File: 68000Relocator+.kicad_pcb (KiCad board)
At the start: 2 copper layers, 97.4 x 94.7 mm, 5 parts, among them J1 5V AUX, P99 OSHW_LOGO, U1 68000D, U2 68000D

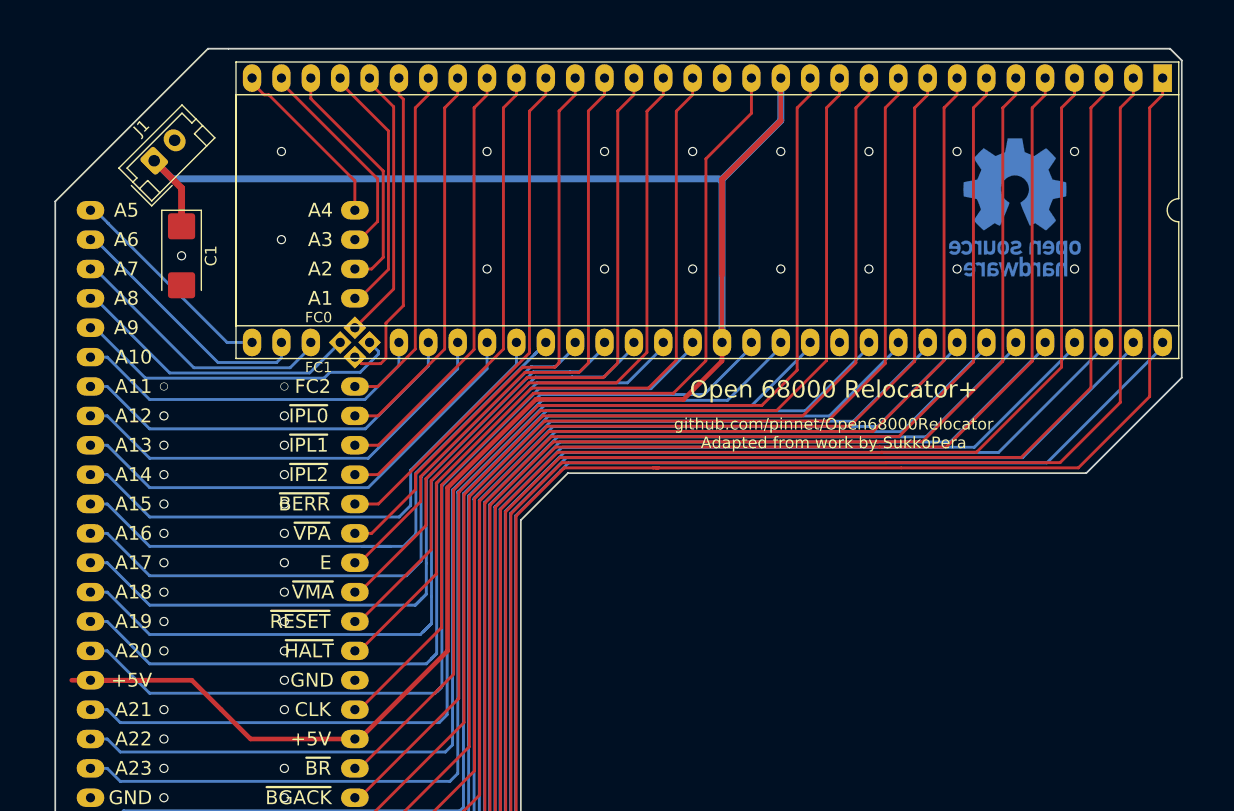
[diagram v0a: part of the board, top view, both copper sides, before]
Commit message: Update design for 3A power delivery thanks to LinuxJedi for the info
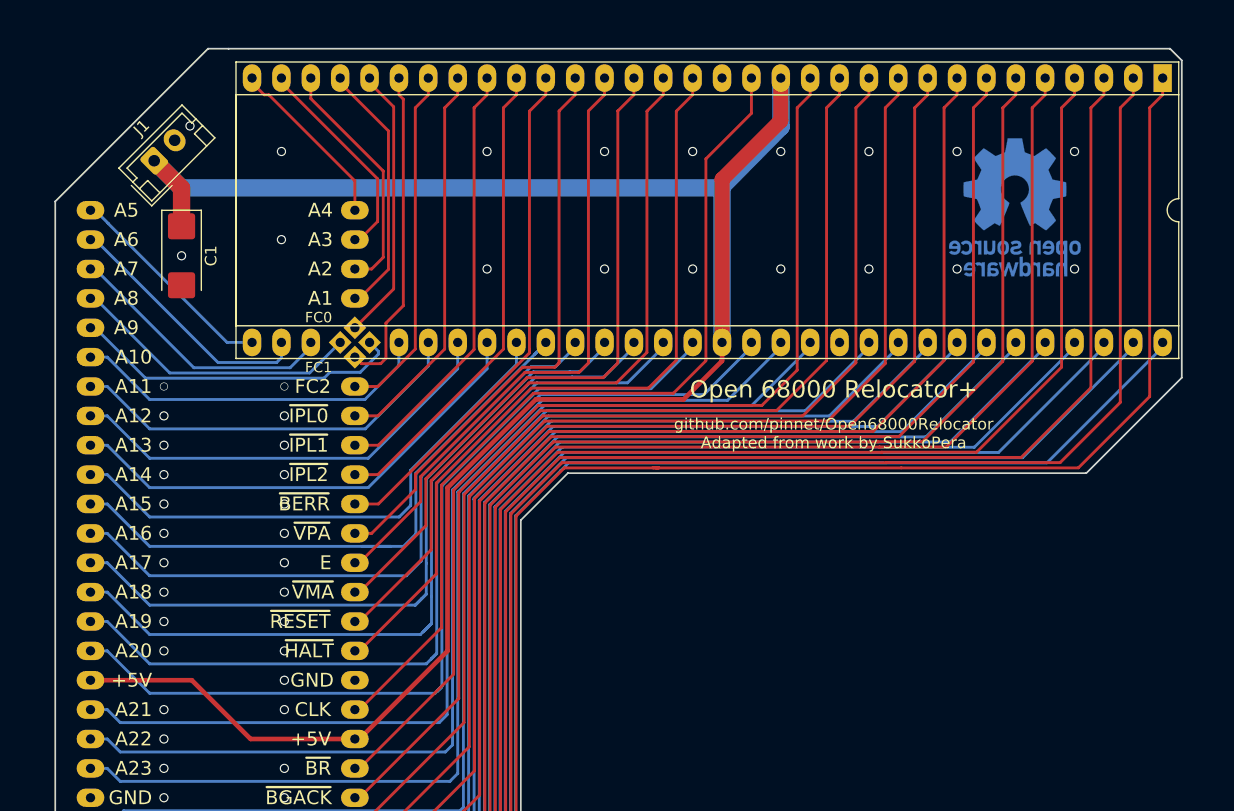
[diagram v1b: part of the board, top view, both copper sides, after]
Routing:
- net VCC: track 193.3 -> 186.8 mm
- net /D7: track 140.7 -> 139.9 mm
- net /BG: track 97.3 -> 96.6 mm
- net GND: vias 71 -> 72
